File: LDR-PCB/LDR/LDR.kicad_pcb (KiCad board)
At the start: 2 copper layers, 6 parts, among them J1 Conn_01x03_Socket, Q1 NPN

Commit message: opamp footprint toegevoegd
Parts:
- added U1: type="X" model="OPAMP" lib="", Package_DIP:DIP-6_W10.16mm, F.Cu at (127.6, 102.5)
- moved R1 6.41 mm to (138.0, 77.1)
- moved R2 3.49 mm to (150.1, 72.5)
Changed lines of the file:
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@@
   (net 6 "Net-(U1--)")
   (footprint "Resistor_THT:R_Axial_DIN0204_L3.6mm_D1.6mm_P5.08mm_Horizontal" (layer "F.Cu")
-    (at 141.95 82.17)
+    (at 138.02 77.1)
     (descr "Resistor, Axial_DIN0204 series, Axial, Horizontal, pin pitch=5.08mm, 0.167W, length*diameter=3.6*1.6mm^2, http://cdn-reichelt.de/documents/datenblatt/B400/1_4W%23YAG.pdf")
     (tags "Resistor Axial_DIN0204 series Axial Horizontal pin pitch 5.08mm 0.167W length 3.6mm diameter 1.6mm")
@@
   )
   (footprint "Resistor_THT:R_Axial_DIN0204_L3.6mm_D1.6mm_P5.08mm_Horizontal" (layer "F.Cu")
-    (at 146.92 74.05)
+    (at 150.07 72.55)
     (descr "Resistor, Axial_DIN0204 series, Axial, Horizontal, pin pitch=5.08mm, 0.167W, length*diameter=3.6*1.6mm^2, http://cdn-reichelt.de/documents/datenblatt/B400/1_4W%23YAG.pdf")
     (tags "Resistor Axial_DIN0204 series Axial Horizontal pin pitch 5.08mm 0.167W length 3.6mm diameter 1.6mm")
@@
         (effects (font (size 1 1) (thickness 0.15)))
     )
-    (fp_text value "R" (at 2.54 1.92) (layer "F.Fab")
+    (fp_text value "R" (at 2.54 1.92) (layer "F.Fab") hide
         (effects (font (size 1 1) (thickness 0.15)))
     )
@@
         (effects (font (size 1 1) (thickness 0.15)))
     )
-    (fp_text value "R" (at 2.54 1.92) (layer "F.Fab")
+    (fp_text value "R" (at 2.54 1.92) (layer "F.Fab") hide
         (effects (font (size 1 1) (thickness 0.15)))
     )
@@
         (effects (font (size 1 1) (thickness 0.15)))
     )
-    (fp_text value "R" (at 2.54 1.92) (layer "F.Fab")
+    (fp_text value "R" (at 2.54 1.92) (layer "F.Fab") hide
         (effects (font (size 1 1) (thickness 0.15)))
     )
@@
     )
   )
+  (footprint "Package_DIP:DIP-6_W10.16mm" (layer "F.Cu")
+    (at 127.6 102.525)
+    (descr "6-lead though-hole mounted DIP package, row spacing 10.16 mm (400 mils)")
+    (tags "THT DIP DIL PDIP 2.54mm 10.16mm 400mil")
+    (property "Sheetfile" "LDR.kicad_sch")
+    (property "Sheetname" "")
+    (property "Sim.Device" "SPICE")
+    (property "Sim.Params" "type=\"X\" model=\"OPAMP\" lib=\"\"")
+    (property "Sim.Pins" "1=1 2=2 3=3 4=4 5=5")
+    (property "ki_description" "Operational amplifier, single, node sequence=1:+ 2:- 3:OUT 4:V+ 5:V-")
+    (property "ki_keywords" "simulation")
+    (attr through_hole)
+    (fp_text reference "U1" (at 5.08 -2.33) (layer "F.SilkS")
+        (effects (font (size 1 1) (thickness 0.15)))
+    )
+    (fp_text value "type=\"X\" model=\"OPAMP\" lib=\"\"" (at 5.08 7.41) (layer "F.Fab") hide
+        (effects (font (size 1 1) (thickness 0.15)))
+    )
+    (fp_text user "${REFERENCE}" (at 5.08 2.54) (layer "F.Fab")
+        (effects (font (size 1 1) (thickness 0.15)))
+    )
+    (fp_line (start 1.845 -1.33) (end 1.845 6.41)
+      (stroke (width 0.12) (type solid)) (layer "F.SilkS"))
+    (fp_line (start 1.845 6.41) (end 8.315 6.41)
+      (stroke (width 0.12) (type solid)) (layer "F.SilkS"))
+    (fp_line (start 4.08 -1.33) (end 1.845 -1.33)
+      (stroke (width 0.12) (type solid)) (layer "F.SilkS"))
+    (fp_line (start 8.315 -1.33) (end 6.08 -1.33)
+      (stroke (width 0.12) (type solid)) (layer "F.SilkS"))
+    (fp_line (start 8.315 6.41) (end 8.315 -1.33)
+      (stroke (width 0.12) (type solid)) (layer "F.SilkS"))
+    (fp_arc (start 6.08 -1.33) (mid 5.08 -0.33) (end 4.08 -1.33)
+      (stroke (width 0.12) (type solid)) (layer "F.SilkS"))
+    (fp_line (start -1.05 -1.55) (end -1.05 6.6)
+      (stroke (width 0.05) (type solid)) (layer "F.CrtYd"))
+    (fp_line (start -1.05 6.6) (end 11.25 6.6)
+      (stroke (width 0.05) (type solid)) (layer "F.CrtYd"))
+    (fp_line (start 11.25 -1.55) (end -1.05 -1.55)
+      (stroke (width 0.05) (type solid)) (layer "F.CrtYd"))
+    (fp_line (start 11.25 6.6) (end 11.25 -1.55)
+      (stroke (width 0.05) (type solid)) (layer "F.CrtYd"))
+    (fp_line (start 1.905 -0.27) (end 2.905 -1.27)
+      (stroke (width 0.1) (type solid)) (layer "F.Fab"))
+    (fp_line (start 1.905 6.35) (end 1.905 -0.27)
+      (stroke (width 0.1) (type solid)) (layer "F.Fab"))
+    (fp_line (start 2.905 -1.27) (end 8.255 -1.27)
+      (stroke (width 0.1) (type solid)) (layer "F.Fab"))
+    (fp_line (start 8.255 -1.27) (end 8.255 6.35)
+      (stroke (width 0.1) (type solid)) (layer "F.Fab"))
+    (fp_line (start 8.255 6.35) (end 1.905 6.35)
+      (stroke (width 0.1) (type solid)) (layer "F.Fab"))
+    (pad "1" thru_hole rect (at 0 0) (size 1.6 1.6) (drill 0.8) (layers "*.Cu" "*.Mask")
+      (net 4 "Net-(U1-+)") (pinfunction "+") (pintype "input"))
+    (pad "2" thru_hole oval (at 0 2.54) (size 1.6 1.6) (drill 0.8) (layers "*.Cu" "*.Mask")
+      (net 6 "Net-(U1--)") (pinfunction "-") (pintype "input"))
+    (pad "3" thru_hole oval (at 0 5.08) (size 1.6 1.6) (drill 0.8) (layers "*.Cu" "*.Mask")
+      (net 2 "Net-(Q1-B)") (pintype "output"))
+    (pad "4" thru_hole oval (at 10.16 5.08) (size 1.6 1.6) (drill 0.8) (layers "*.Cu" "*.Mask")
+      (net 3 "+3V3") (pinfunction "V+") (pintype "power_in"))
+    (pad "5" thru_hole oval (at 10.16 2.54) (size 1.6 1.6) (drill 0.8) (layers "*.Cu" "*.Mask")
+      (net 5 "GND") (pinfunction "V-") (pintype "power_in"))
+    (pad "6" thru_hole oval (at 10.16 0) (size 1.6 1.6) (drill 0.8) (layers "*.Cu" "*.Mask"))
+    (model "${KICAD6_3DMODEL_DIR}/Package_DIP.3dshapes/DIP-6_W10.16mm.wrl"
+      (offset (xyz 0 0 0))
+      (scale (xyz 1 1 1))
+      (rotate (xyz 0 0 0))
+    )
+  )
   (footprint "Connector_PinSocket_2.00mm:PinSocket_1x03_P2.00mm_Vertical" (layer "F.Cu")
     (at 153.37 85.6)
@@
         (effects (font (size 1 1) (thickness 0.15)))
     )
-    (fp_text value "Conn_01x03_Socket" (at 0 6.5) (layer "F.Fab")
-        (effects (font (size 1 1) (thickness 0.15)))
-    )
+    (fp_text value "Conn_01x03_Socket" (at 0 6.5) (layer "F.Fab") hide
+        (effects (font (size 1 1) (thickness 0.15)))
+    )

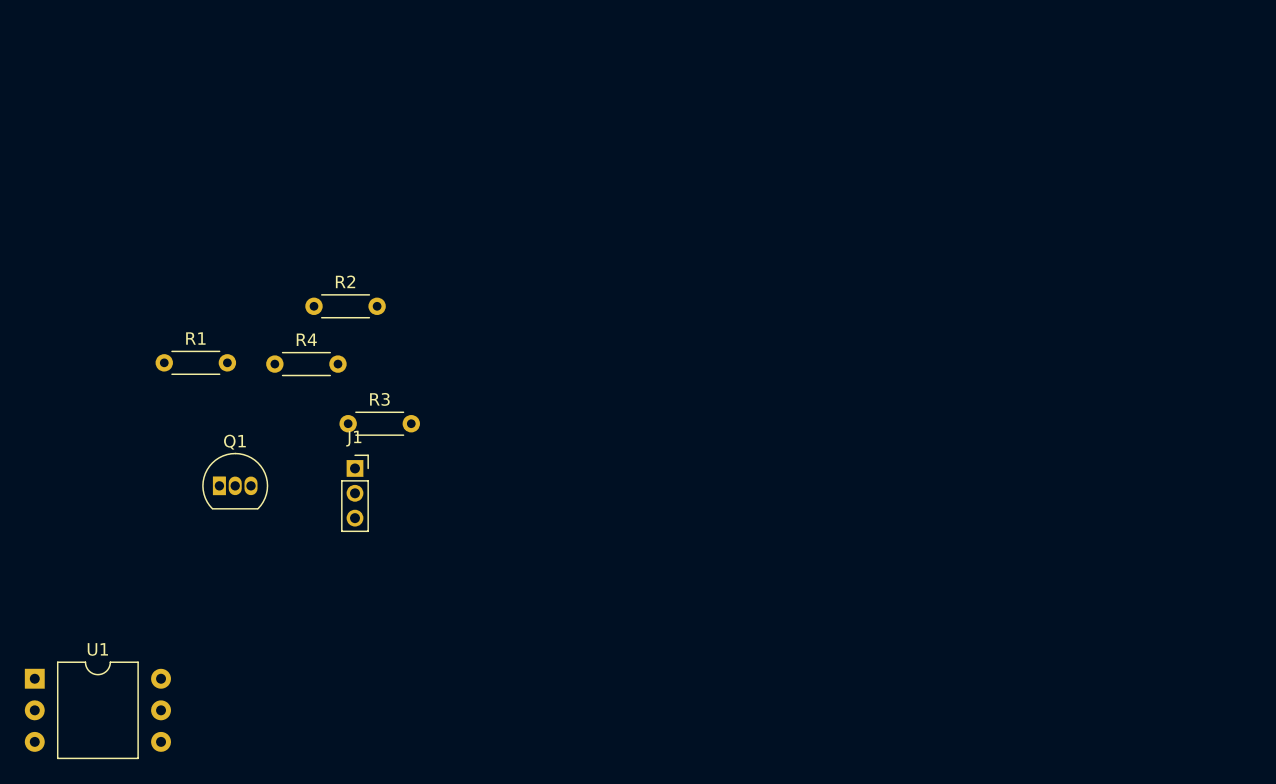
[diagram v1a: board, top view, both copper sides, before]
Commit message: LDR zal nu de 3v3_en omlaag trekken om de pico uit te zetten
Gedeeltelijke merge
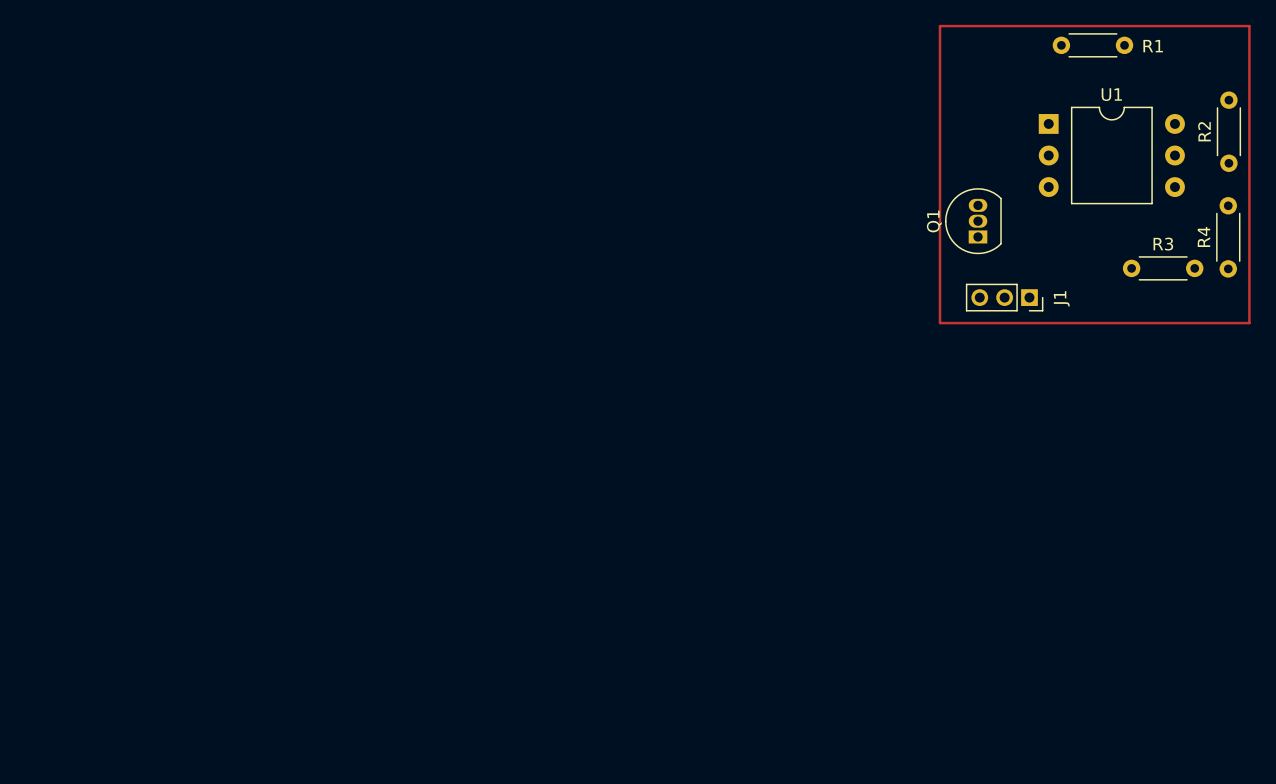
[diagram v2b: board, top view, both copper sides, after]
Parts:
- moved U1 93.0 mm to (209.2, 57.9)
- moved R4 77.1 mm to (223.7, 69.5), turned to 90 degrees
- moved R1 76.6 mm to (210.2, 51.5)
- moved R2 74.5 mm to (223.7, 61.0), turned to 90 degrees
- moved R3 64.3 mm to (215.9, 69.5)
- moved Q1 64.3 mm to (203.5, 67.0), turned to 90 degrees
- moved J1 56.0 mm to (207.7, 71.8), turned to -90 degrees
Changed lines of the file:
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@@
   (net 6 "Net-(U1--)")
   (footprint "Resistor_THT:R_Axial_DIN0204_L3.6mm_D1.6mm_P5.08mm_Horizontal" (layer "F.Cu")
-    (at 138.02 77.1)
+    (at 210.22 51.55)
     (descr "Resistor, Axial_DIN0204 series, Axial, Horizontal, pin pitch=5.08mm, 0.167W, length*diameter=3.6*1.6mm^2, http://cdn-reichelt.de/documents/datenblatt/B400/1_4W%23YAG.pdf")
     (tags "Resistor Axial_DIN0204 series Axial Horizontal pin pitch 5.08mm 0.167W length 3.6mm diameter 1.6mm")
@@
     (property "ki_keywords" "resistor variable light sensitive opto LDR")
     (attr through_hole)
-    (fp_text reference "R1" (at 2.54 -1.92) (layer "F.SilkS")
+    (fp_text reference "R1" (at 7.38 0.1) (layer "F.SilkS")
         (effects (font (size 1 1) (thickness 0.15)))
     )
@@
   )
   (footprint "Resistor_THT:R_Axial_DIN0204_L3.6mm_D1.6mm_P5.08mm_Horizontal" (layer "F.Cu")
-    (at 150.07 72.55)
+    (at 223.7 61.04 90)
     (descr "Resistor, Axial_DIN0204 series, Axial, Horizontal, pin pitch=5.08mm, 0.167W, length*diameter=3.6*1.6mm^2, http://cdn-reichelt.de/documents/datenblatt/B400/1_4W%23YAG.pdf")
     (tags "Resistor Axial_DIN0204 series Axial Horizontal pin pitch 5.08mm 0.167W length 3.6mm diameter 1.6mm")
@@
     (property "ki_keywords" "R res resistor")
     (attr through_hole)
-    (fp_text reference "R2" (at 2.54 -1.92) (layer "F.SilkS")
-        (effects (font (size 1 1) (thickness 0.15)))
-    )
-    (fp_text value "R" (at 2.54 1.92) (layer "F.Fab") hide
-        (effects (font (size 1 1) (thickness 0.15)))
-    )
-    (fp_text user "${REFERENCE}" (at 2.54 0) (layer "F.Fab")
+    (fp_text reference "R2" (at 2.54 -1.92 90) (layer "F.SilkS")
+        (effects (font (size 1 1) (thickness 0.15)))
+    )
+    (fp_text value "R" (at 2.54 1.92 90) (layer "F.Fab") hide
+        (effects (font (size 1 1) (thickness 0.15)))
+    )
+    (fp_text user "${REFERENCE}" (at 2.54 0 90) (layer "F.Fab")
         (effects (font (size 0.72 0.72) (thickness 0.108)))
     )
@@
     (fp_line (start 5.08 0) (end 4.34 0)
       (stroke (width 0.1) (type solid)) (layer "F.Fab"))
-    (pad "1" thru_hole circle (at 0 0) (size 1.4 1.4) (drill 0.7) (layers "*.Cu" "*.Mask")
+    (pad "1" thru_hole circle (at 0 0 90) (size 1.4 1.4) (drill 0.7) (layers "*.Cu" "*.Mask")
       (net 3 "+3V3") (pintype "passive"))
-    (pad "2" thru_hole oval (at 5.08 0) (size 1.4 1.4) (drill 0.7) (layers "*.Cu" "*.Mask")
+    (pad "2" thru_hole oval (at 5.08 0 90) (size 1.4 1.4) (drill 0.7) (layers "*.Cu" "*.Mask")
       (net 4 "Net-(U1-+)") (pintype "passive"))
     (model "${KICAD6_3DMODEL_DIR}/Resistor_THT.3dshapes/R_Axial_DIN0204_L3.6mm_D1.6mm_P5.08mm_Horizontal.wrl"
@@
   )
   (footprint "Resistor_THT:R_Axial_DIN0204_L3.6mm_D1.6mm_P5.08mm_Horizontal" (layer "F.Cu")
-    (at 152.82 82)
+    (at 215.87 69.5)
     (descr "Resistor, Axial_DIN0204 series, Axial, Horizontal, pin pitch=5.08mm, 0.167W, length*diameter=3.6*1.6mm^2, http://cdn-reichelt.de/documents/datenblatt/B400/1_4W%23YAG.pdf")
     (tags "Resistor Axial_DIN0204 series Axial Horizontal pin pitch 5.08mm 0.167W length 3.6mm diameter 1.6mm")
@@
   )
   (footprint "Resistor_THT:R_Axial_DIN0204_L3.6mm_D1.6mm_P5.08mm_Horizontal" (layer "F.Cu")
-    (at 146.92 77.2)
+    (at 223.65 69.54 90)
     (descr "Resistor, Axial_DIN0204 series, Axial, Horizontal, pin pitch=5.08mm, 0.167W, length*diameter=3.6*1.6mm^2, http://cdn-reichelt.de/documents/datenblatt/B400/1_4W%23YAG.pdf")
     (tags "Resistor Axial_DIN0204 series Axial Horizontal pin pitch 5.08mm 0.167W length 3.6mm diameter 1.6mm")
@@
     (property "ki_keywords" "R res resistor")
     (attr through_hole)
-    (fp_text reference "R4" (at 2.54 -1.92) (layer "F.SilkS")
-        (effects (font (size 1 1) (thickness 0.15)))
-    )
-    (fp_text value "R" (at 2.54 1.92) (layer "F.Fab") hide
-        (effects (font (size 1 1) (thickness 0.15)))
-    )
-    (fp_text user "${REFERENCE}" (at 2.54 0) (layer "F.Fab")
+    (fp_text reference "R4" (at 2.54 -1.92 90) (layer "F.SilkS")
+        (effects (font (size 1 1) (thickness 0.15)))
+    )
+    (fp_text value "R" (at 2.54 1.92 90) (layer "F.Fab") hide
+        (effects (font (size 1 1) (thickness 0.15)))
+    )
+    (fp_text user "${REFERENCE}" (at 2.54 0 90) (layer "F.Fab")
         (effects (font (size 0.72 0.72) (thickness 0.108)))
     )
@@
     (fp_line (start 5.08 0) (end 4.34 0)
       (stroke (width 0.1) (type solid)) (layer "F.Fab"))
-    (pad "1" thru_hole circle (at 0 0) (size 1.4 1.4) (drill 0.7) (layers "*.Cu" "*.Mask")
+    (pad "1" thru_hole circle (at 0 0 90) (size 1.4 1.4) (drill 0.7) (layers "*.Cu" "*.Mask")
       (net 6 "Net-(U1--)") (pintype "passive"))
-    (pad "2" thru_hole oval (at 5.08 0) (size 1.4 1.4) (drill 0.7) (layers "*.Cu" "*.Mask")
+    (pad "2" thru_hole oval (at 5.08 0 90) (size 1.4 1.4) (drill 0.7) (layers "*.Cu" "*.Mask")
       (net 5 "GND") (pintype "passive"))
     (model "${KICAD6_3DMODEL_DIR}/Resistor_THT.3dshapes/R_Axial_DIN0204_L3.6mm_D1.6mm_P5.08mm_Horizontal.wrl"
@@
   )
   (footprint "Package_TO_SOT_THT:TO-92_Inline" (layer "F.Cu")
-    (at 142.46 87)
+    (at 203.51 66.97 90)
     (descr "TO-92 leads in-line, narrow, oval pads, drill 0.75mm (see NXP sot054_po.pdf)")
     (tags "to-92 sc-43 sc-43a sot54 PA33 transistor")
@@
     (property "ki_keywords" "NPN Transistor")
     (attr through_hole)
-    (fp_text reference "Q1" (at 1.27 -3.56) (layer "F.SilkS")
-        (effects (font (size 1 1) (thickness 0.15)))
-    )
-    (fp_text value "NPN" (at 1.27 2.79) (layer "F.Fab")
-        (effects (font (size 1 1) (thickness 0.15)))
-    )
-    (fp_text user "${REFERENCE}" (at 1.27 0) (layer "F.Fab")
+    (fp_text reference "Q1" (at 1.27 -3.56 90) (layer "F.SilkS")
+        (effects (font (size 1 1) (thickness 0.15)))
+    )
+    (fp_text value "NPN" (at 1.27 2.79 90) (layer "F.Fab")
+        (effects (font (size 1 1) (thickness 0.15)))
+    )
+    (fp_text user "${REFERENCE}" (at 1.27 0 90) (layer "F.Fab")
         (effects (font (size 1 1) (thickness 0.15)))
     )
@@
     (fp_arc (start 1.27 -2.48) (mid 3.561221 -0.949055) (end 3.023625 1.753625)
       (stroke (width 0.1) (type solid)) (layer "F.Fab"))
-    (pad "1" thru_hole rect (at 0 0) (size 1.05 1.5) (drill 0.75) (layers "*.Cu" "*.Mask")
+    (pad "1" thru_hole rect (at 0 0 90) (size 1.05 1.5) (drill 0.75) (layers "*.Cu" "*.Mask")
       (net 1 "OUT") (pinfunction "E") (pintype "passive"))
-    (pad "2" thru_hole oval (at 1.27 0) (size 1.05 1.5) (drill 0.75) (layers "*.Cu" "*.Mask")
+    (pad "2" thru_hole oval (at 1.27 0 90) (size 1.05 1.5) (drill 0.75) (layers "*.Cu" "*.Mask")
       (net 2 "Net-(Q1-B)") (pinfunction "B") (pintype "input"))
-    (pad "3" thru_hole oval (at 2.54 0) (size 1.05 1.5) (drill 0.75) (layers "*.Cu" "*.Mask")
+    (pad "3" thru_hole oval (at 2.54 0 90) (size 1.05 1.5) (drill 0.75) (layers "*.Cu" "*.Mask")
       (net 3 "+3V3") (pinfunction "C") (pintype "passive"))
     (model "${KICAD6_3DMODEL_DIR}/Package_TO_SOT_THT.3dshapes/TO-92_Inline.wrl"
@@
   )
   (footprint "Package_DIP:DIP-6_W10.16mm" (layer "F.Cu")
-    (at 127.6 102.525)
+    (at 209.2 57.875)
     (descr "6-lead though-hole mounted DIP package, row spacing 10.16 mm (400 mils)")
     (tags "THT DIP DIL PDIP 2.54mm 10.16mm 400mil")
@@
   )
   (footprint "Connector_PinSocket_2.00mm:PinSocket_1x03_P2.00mm_Vertical" (layer "F.Cu")
-    (at 153.37 85.6)
+    (at 207.65 71.85 -90)
     (descr "Through hole straight socket strip, 1x03, 2.00mm pitch, single row (from Kicad 4.0.7), script generated")
     (tags "Through hole socket strip THT 1x03 2.00mm single row")
@@
     (property "ki_keywords" "connector")
     (attr through_hole)
-    (fp_text reference "J1" (at 0 -2.5) (layer "F.SilkS")
-        (effects (font (size 1 1) (thickness 0.15)))
-    )
-    (fp_text value "Conn_01x03_Socket" (at 0 6.5) (layer "F.Fab") hide
-        (effects (font (size 1 1) (thickness 0.15)))
-    )
-    (fp_text user "${REFERENCE}" (at 0 2 90) (layer "F.Fab")
+    (fp_text reference "J1" (at 0 -2.5 90) (layer "F.SilkS")
+        (effects (font (size 1 1) (thickness 0.15)))
+    )
+    (fp_text value "Conn_01x03_Socket" (at 0 6.5 90) (layer "F.Fab") hide
+        (effects (font (size 1 1) (thickness 0.15)))
+    )
+    (fp_text user "${REFERENCE}" (at 0 2) (layer "F.Fab")
         (effects (font (size 1 1) (thickness 0.15)))
     )
@@
     (fp_line (start 1 5) (end -1 5)
       (stroke (width 0.1) (type solid)) (layer "F.Fab"))
-    (pad "1" thru_hole rect (at 0 0) (size 1.35 1.35) (drill 0.8) (layers "*.Cu" "*.Mask")
+    (pad "1" thru_hole rect (at 0 0 270) (size 1.35 1.35) (drill 0.8) (layers "*.Cu" "*.Mask")
       (net 3 "+3V3") (pinfunction "Pin_1") (pintype "passive"))
-    (pad "2" thru_hole oval (at 0 2) (size 1.35 1.35) (drill 0.8) (layers "*.Cu" "*.Mask")
+    (pad "2" thru_hole oval (at 0 2 270) (size 1.35 1.35) (drill 0.8) (layers "*.Cu" "*.Mask")
       (net 5 "GND") (pinfunction "Pin_2") (pintype "passive"))
-    (pad "3" thru_hole oval (at 0 4) (size 1.35 1.35) (drill 0.8) (layers "*.Cu" "*.Mask")
+    (pad "3" thru_hole oval (at 0 4 270) (size 1.35 1.35) (drill 0.8) (layers "*.Cu" "*.Mask")
       (net 1 "OUT") (pinfunction "Pin_3") (pintype "passive"))
     (model "${KICAD6_3DMODEL_DIR}/Connector_PinSocket_2.00mm.3dshapes/PinSocket_1x03_P2.00mm_Vertical.wrl"
@@
     )
   )
+  (gr_rect (start 200.45 50) (end 225.35 73.9)
+    (stroke (width 0.2) (type default)) (fill none) (layer "F.Cu"))
 )

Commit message: PCB LDR af (bijna)
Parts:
- added H1: MountingHole_Pad, MountingHole:MountingHole_2.2mm_M2_ISO14580_Pad, F.Cu at (203.2, 54.9)
- added H2: MountingHole_Pad, MountingHole:MountingHole_2.2mm_M2_ISO14580_Pad, F.Cu at (220.9, 70.3)
- U1: footprint Package_DIP:DIP-6_W10.16mm -> Package_DIP:DIP-8_W7.62mm
- moved R4 9.11 mm to (219.0, 61.7), turned to -90 degrees
- moved J1 4.97 mm to (202.8, 70.8), turned to 180 degrees
- moved R2 4.95 mm to (218.9, 59.6)
- moved Q1 3.91 mm to (204.2, 63.1)
- moved R1 2.17 mm to (209.5, 53.6)
- moved R3 1.79 mm to (214.2, 68.8), turned to 180 degrees
- moved U1 1.22 mm to (208.0, 57.6)
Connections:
- J1 pad 3: OUT -> 3V3_en
- Q1 pad 1: OUT -> GND
- Q1 pad 3: +3V3 -> 3V3_en
- R1 pad 1: Net-(U1-+) -> Net-(U1--A)
- R2 pad 2: Net-(U1-+) -> Net-(U1-+A)
- R3 pad 2: Net-(U1--) -> Net-(U1--A)
- R4 pad 1: Net-(U1--) -> Net-(U1-+A)
- U1 pad 1: Net-(U1-+) -> Net-(Q1-B)
- U1 pad 2: Net-(U1--) -> Net-(U1--A)
- U1 pad 3: Net-(Q1-B) -> Net-(U1-+A)
- U1 pad 4: +3V3 -> GND
- U1 pad 5: GND -> (no net)
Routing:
- net +3V3: track 0.00 -> 28.9 mm
- net Net-(U1-+A): track 0.00 -> 22.7 mm
- net Net-(U1--A): track 0.00 -> 17.9 mm
- net 3V3_en: track 0.00 -> 7.48 mm
- net Net-(Q1-B): track 0.00 -> 5.86 mm
- added copper zone on B.Cu, net GND

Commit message: LDR board is af
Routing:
- net 3V3_en: track 7.48 -> 8.77 mm
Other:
- board outline added: 22.6 x 20.4 mm
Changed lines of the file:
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@@
     )
   )
-  (gr_rect (start 200.55 52.35) (end 223.55 73)
-    (stroke (width 0.2) (type default)) (fill none) (layer "F.Cu"))
-  (segment (start 202.8 61.765) (end 202.8 66.75) (width 0.25) (layer "F.Cu") (net 1))
+  (gr_rect (start 200.8 52.5) (end 223.4 72.9)
+    (stroke (width 0.1) (type default)) (fill none) (layer "Edge.Cuts"))
+  (segment (start 202.2 66.15) (end 202.8 66.75) (width 0.25) (layer "F.Cu") (net 1))
+  (segment (start 203.965 60.6) (end 202.7 60.6) (width 0.25) (layer "F.Cu") (net 1))
+  (segment (start 202.7 60.6) (end 202.3 61) (width 0.25) (layer "F.Cu") (net 1))
+  (segment (start 202.3 61) (end 202.2 61) (width 0.25) (layer "F.Cu") (net 1))
+  (segment (start 202.2 61) (end 202.2 66.15) (width 0.25) (layer "F.Cu") (net 1))
   (segment (start 204.21 60.58) (end 203.985 60.58) (width 0.25) (layer "F.Cu") (net 1))
-  (segment (start 203.985 60.58) (end 202.8 61.765) (width 0.25) (layer "F.Cu") (net 1))
+  (segment (start 203.985 60.58) (end 203.965 60.6) (width 0.25) (layer "F.Cu") (net 1))
   (segment (start 203.62 60.58) (end 204.21 60.58) (width 0.25) (layer "B.Cu") (net 1))
   (segment (start 204.367082 61.85) (end 204.21 61.85) (width 0.25) (layer "F.Cu") (net 2))
